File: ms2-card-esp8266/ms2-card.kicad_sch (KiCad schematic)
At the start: 58 parts, among them J1 Schaltregler, J10 MicroSD_SPI_CD, J11 Conn_01x06, J2 ESP Prog, J20 Smartcard Connector, J21 PogoPin, J22 Card Edge, J23 Conn_01x04, J30 USB_B_Micro, J31 Power Select, J32 Conn_01x03, Q1 MMBT3904, Q2 MMBT3904, SW1 RESET, U1 ESP-12F, U2 FM24C64B, U20 BL1551B, U3 BL1551B, U30 CP2102N-Axx-xQFN24, U4 BL1551B, U6 AMS1117-3.3

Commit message: in production
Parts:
- R1, R31, R32, R7: LCSC C23018 -> C23138
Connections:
- net Card: now also U1.22 (SCLK)
- no-connect marks 24 -> 23
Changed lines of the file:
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@@
   (no_connect (at 263.652 51.054))
   (no_connect (at 222.25 53.594))
-  (no_connect (at 93.98 125.73))
   (no_connect (at 222.25 66.294))
   (no_connect (at 135.89 32.766))
@@
     (stroke (width 0) (type default) (color 0 0 0 0))
   )
+  (wire (pts (xy 93.98 125.73) (xy 104.14 125.73))
+    (stroke (width 0) (type default) (color 0 0 0 0))
+  )
   (wire (pts (xy 271.272 56.134) (xy 271.272 57.404))
     (stroke (width 0) (type default) (color 0 0 0 0))
@@
   (label "TxD" (at 215.646 33.274 0)
     (effects (font (size 1.27 1.27)) (justify left bottom))
+  )
+  (label "Card" (at 104.14 125.73 180)
+    (effects (font (size 1.27 1.27)) (justify right bottom))
   )
   (label "MISO" (at 59.69 107.95 0)
@@
       (effects (font (size 1.27 1.27)) hide)
     )
-    (property "LCSC" "C23018" (id 4) (at 73.914 25.781 0)
+    (property "LCSC" "C23138" (id 4) (at 73.914 25.781 0)
       (effects (font (size 1.27 1.27)) hide)
     )
@@
       (effects (font (size 1.27 1.27)) hide)
     )
-    (property "LCSC" "C23018" (id 4) (at 60.96 65.405 0)
+    (property "LCSC" "C23138" (id 4) (at 60.96 65.405 0)
       (effects (font (size 1.27 1.27)) hide)
     )
@@
       (effects (font (size 1.27 1.27)) hide)
     )
-    (property "LCSC" "C23018" (id 4) (at 206.502 76.454 0)
+    (property "LCSC" "C23138" (id 4) (at 206.502 76.454 0)
       (effects (font (size 1.27 1.27)) hide)
     )
@@
       (effects (font (size 1.27 1.27)) hide)
     )
-    (property "LCSC" "C23018" (id 4) (at 192.278 76.708 0)
-      (effects (font (size 1.27 1.27)) hide)
-    )
+    (property "LCSC" "C23138" (id 4) (at 192.278 76.708 0)
+      (effects (font (size 1.27 1.27)) hide)
+    )

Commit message: first production
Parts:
- R11, R12, R13, R2, R20, R21, R22, R23, R5, R6: LCSC C17673 -> C23162
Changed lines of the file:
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@@
       (effects (font (size 1.27 1.27)) hide)
     )
-    (property "LCSC" "C17673" (id 4) (at 216.408 141.351 90)
+    (property "LCSC" "C23162" (id 4) (at 216.408 141.351 90)
       (effects (font (size 1.27 1.27)) hide)
     )
@@
       (effects (font (size 1.27 1.27)) hide)
     )
-    (property "LCSC" "C17673" (id 4) (at 219.583 141.351 90)
+    (property "LCSC" "C23162" (id 4) (at 219.583 141.351 90)
       (effects (font (size 1.27 1.27)) hide)
     )
@@
       (effects (font (size 1.27 1.27)) hide)
     )
-    (property "LCSC" "C17673" (id 4) (at 222.758 141.351 90)
+    (property "LCSC" "C23162" (id 4) (at 222.758 141.351 90)
       (effects (font (size 1.27 1.27)) hide)
     )
@@
       (effects (font (size 1.27 1.27)) hide)
     )
-    (property "LCSC" "C17673" (id 4) (at 141.732 119.888 90)
+    (property "LCSC" "C23162" (id 4) (at 141.732 119.888 90)
       (effects (font (size 1.27 1.27)) hide)
     )
@@
       (effects (font (size 1.27 1.27)) hide)
     )
-    (property "LCSC" "C17673" (id 4) (at 144.907 119.888 90)
+    (property "LCSC" "C23162" (id 4) (at 144.907 119.888 90)
       (effects (font (size 1.27 1.27)) hide)
     )
@@
       (effects (font (size 1.27 1.27)) hide)
     )
-    (property "LCSC" "C17673" (id 4) (at 115.57 116.84 90)
+    (property "LCSC" "C23162" (id 4) (at 115.57 116.84 90)
       (effects (font (size 1.27 1.27)) hide)
     )
@@
       (effects (font (size 1.27 1.27)) hide)
     )
-    (property "LCSC" "C17673" (id 4) (at 153.035 119.761 90)
+    (property "LCSC" "C23162" (id 4) (at 153.035 119.761 90)
       (effects (font (size 1.27 1.27)) hide)
     )
@@
       (effects (font (size 1.27 1.27)) hide)
     )
-    (property "LCSC" "C17673" (id 4) (at 156.21 119.761 90)
+    (property "LCSC" "C23162" (id 4) (at 156.21 119.761 90)
       (effects (font (size 1.27 1.27)) hide)
     )
@@
       (effects (font (size 1.27 1.27)) hide)
     )
-    (property "LCSC" "C17673" (id 4) (at 128.651 120.904 90)
+    (property "LCSC" "C23162" (id 4) (at 128.651 120.904 90)
       (effects (font (size 1.27 1.27)) hide)
     )
@@
       (effects (font (size 1.27 1.27)) hide)
     )
-    (property "LCSC" "C17673" (id 4) (at 131.826 120.904 90)
-      (effects (font (size 1.27 1.27)) hide)
-    )
+    (property "LCSC" "C23162" (id 4) (at 131.826 120.904 90)
+      (effects (font (size 1.27 1.27)) hide)
+    )

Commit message: replace SW1 / calm down DRC - part I
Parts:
- SW1: footprint w_switch:PCB_PUSH -> Button_Switch_THT:SW_PUSH_6mm_H4.3mm
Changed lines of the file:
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@@
     (property "Reference" "SW1" (id 0) (at 46.355 88.011 0))
     (property "Value" "RESET" (id 1) (at 46.355 90.3224 0))
-    (property "Footprint" "w_switch:PCB_PUSH" (id 2) (at 46.355 90.17 0)
+    (property "Footprint" "Button_Switch_THT:SW_PUSH_6mm_H4.3mm" (id 2) (at 46.355 90.17 0)
       (effects (font (size 1.27 1.27)) hide)
     )
@@
     )
     (path "/00000000-0000-0000-0000-00006210c221"
-      (reference "SW1") (unit 1) (value "RESET") (footprint "w_switch:PCB_PUSH")
+      (reference "SW1") (unit 1) (value "RESET") (footprint "Button_Switch_THT:SW_PUSH_6mm_H4.3mm")
     )
     (path "/00000000-0000-0000-0000-00006208ee80"

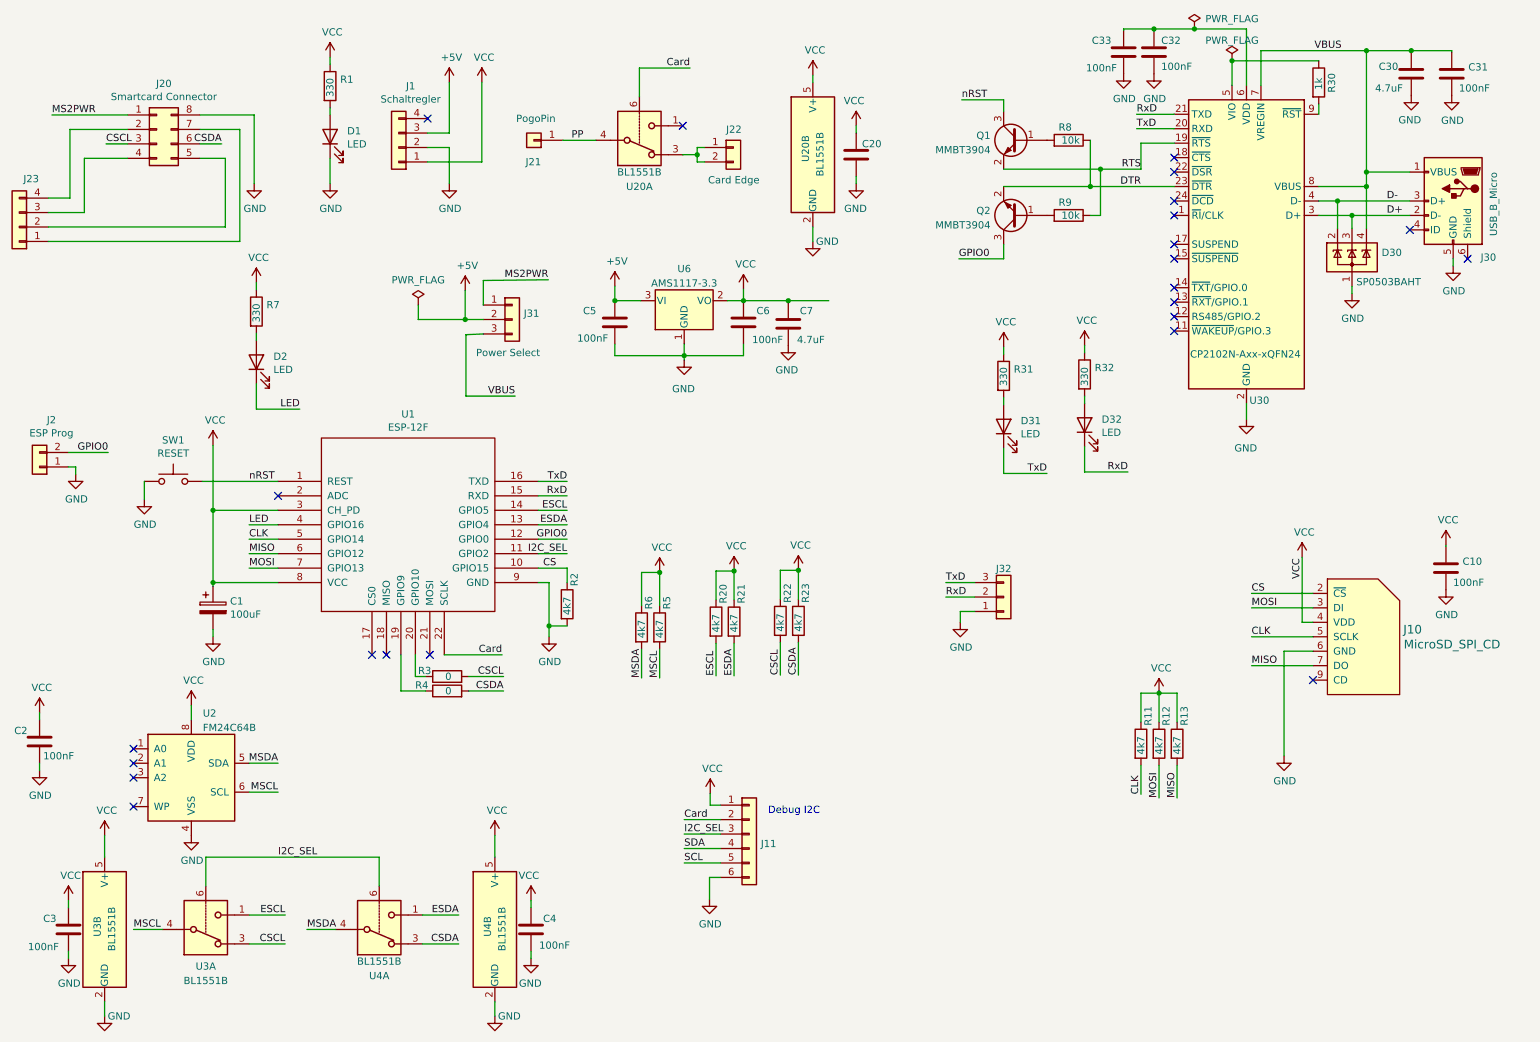
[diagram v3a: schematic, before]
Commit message: replace ESP8266 footprint with standard KiCAD
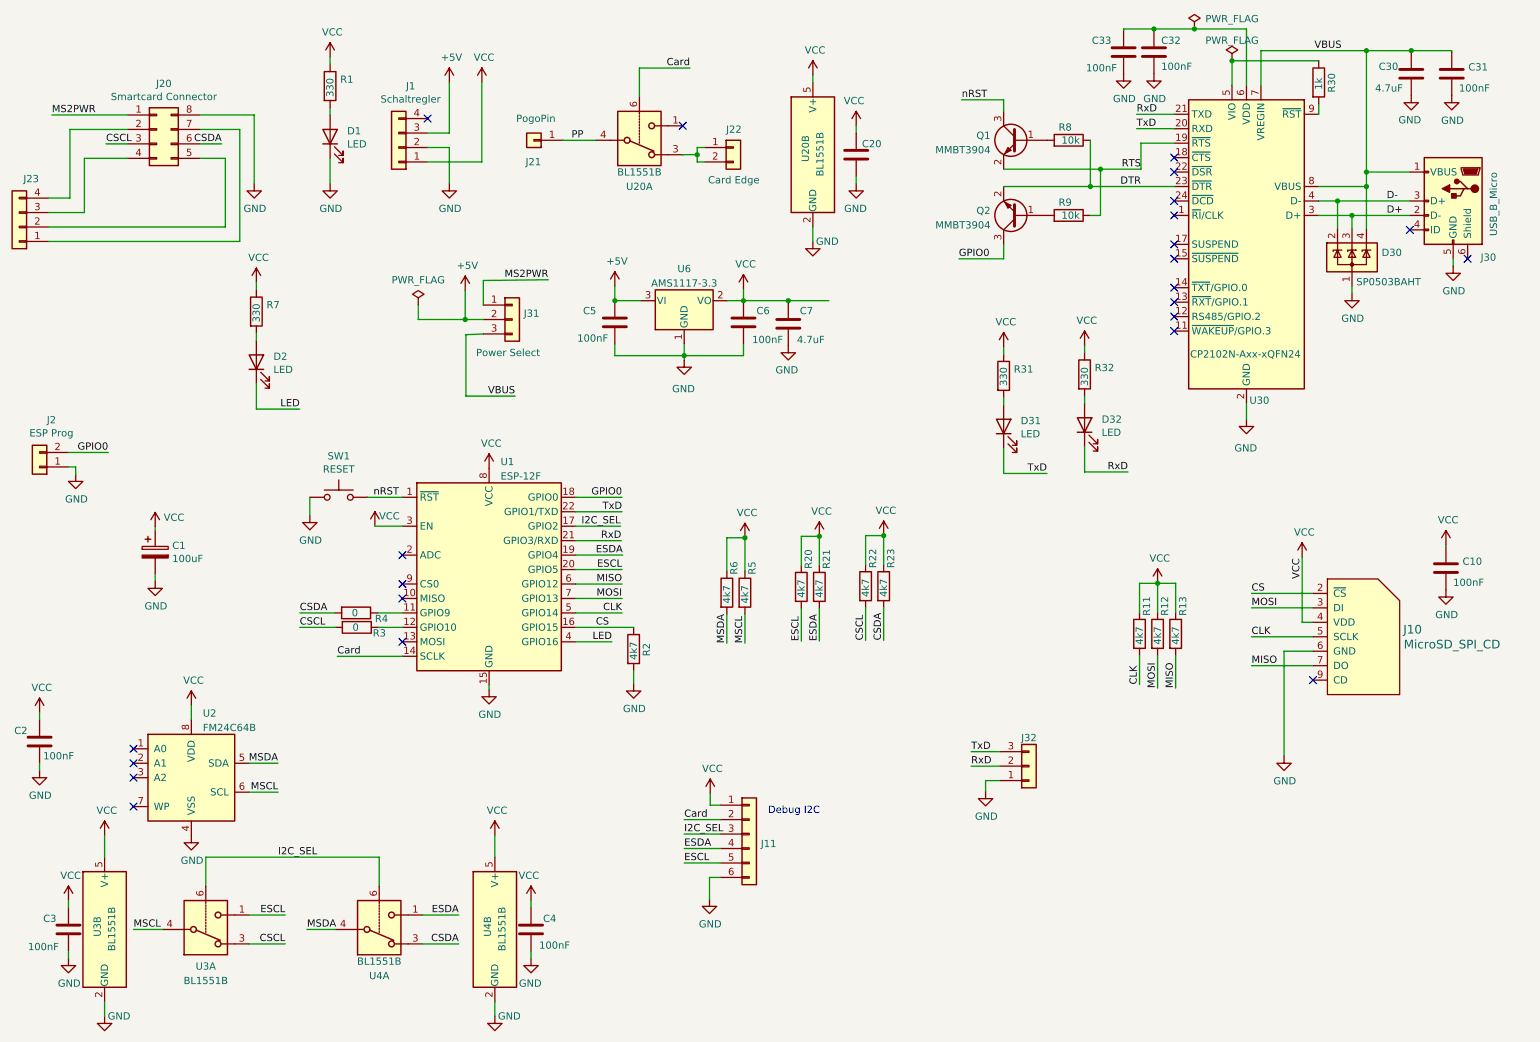
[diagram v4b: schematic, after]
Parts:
- removed U1: ESP-12F, ESP8266:ESP-12E, symbol ms2-card-rescue:ESP-12F-ESP8266
- added U1: ESP-12F, RF_Module:ESP-12E, symbol RF_Module:ESP-12E
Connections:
- net SCL is gone; now on net ESCL: J11.5 (Pin_5)
- net SDA is gone; now on net ESDA: J11.4 (Pin_4)
- net CLK: now also U1.5 (GPIO14)
- net CS: now also U1.16 (GPIO15)
- net Card: now also U1.14 (SCLK)
- net ESCL: now also U1.20 (GPIO5)
- net ESDA: now also U1.19 (GPIO4)
- net GND: now also U1.15 (GND)
- net GPIO0: now also U1.18 (GPIO0)
- net I2C_SEL: now also U1.17 (GPIO2)
- net LED: now also U1.4 (GPIO16)
- net MISO: now also U1.6 (GPIO12)
- net MOSI: now also U1.7 (GPIO13)
- net RxD: now also U1.21 (GPIO3/RXD)
- net TxD: now also U1.22 (GPIO1/TXD)
- net VCC: now also U1.3 (EN), U1.8 (VCC)
- net nRST: now also U1.1 (~{RST})
- net at R4.1: now also U1.11 (GPIO9)
- net at R3.1: now also U1.12 (GPIO10)
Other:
- moved on the sheet: C1, J32, R11, R12, R13, R2, R20, R21, R22, R23, R3, R4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
